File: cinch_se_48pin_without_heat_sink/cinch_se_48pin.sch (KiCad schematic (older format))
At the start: 1 part, among them P1 Conn48pin

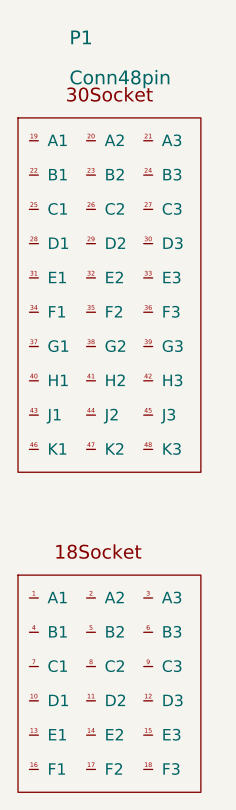
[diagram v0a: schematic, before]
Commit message: Fix schema symbol, 18 and 30 socket were reversed
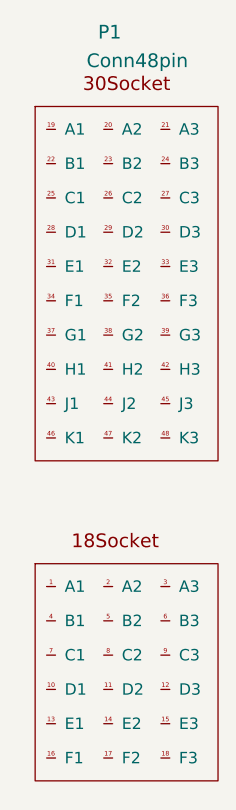
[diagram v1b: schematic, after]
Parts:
- P1: footprint cinch:Conn48pin -> (none)
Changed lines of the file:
@@
 LIBS:valves
 LIBS:cinch
+LIBS:cinch_se_48pin-cache
 EELAYER 25 0
 EELAYER END
@@
 $Comp
 L Conn48pin P1
-U 1 1 56FAE790
-P 925 2300
-F 0 "P1" H 750 3950 60  0000 L CNN
-F 1 "Conn48pin" H 750 3775 60  0000 L CNN
-F 2 "cinch:Conn48pin" H 1075 1300 60  0001 C CNN
-F 3 "http://www.cinch.com/pdfs/1219440691-5810148005s_rev_D.pdf" H 1075 1300 60  0001 C CNN
-	1    925  2300
+U 1 1 56FEA9A7
+P 1000 2250
+F 0 "P1" H 875 3875 60  0000 L CNN
+F 1 "Conn48pin" H 825 3750 60  0000 L CNN
+F 2 "" H 1150 2550 60  0000 C CNN
+F 3 "" H 1150 2550 60  0000 C CNN
+	1    1000 2250
 	1    0    0    -1
 $EndComp
